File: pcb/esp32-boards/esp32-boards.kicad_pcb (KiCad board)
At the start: 2 copper layers, 55 x 48 mm, 45 parts, among them J1 BOOT_MODE, J2 USB_B_Micro, J3 BATTERY, Q1 Q_Photo_NPN, SW1 RESET, SW2 BAT_EN, U1 ESP32-C3-WROOM-02, U2 MAX40200AUK, U3 MCP73831-2-OT, U4 LD39150DT33

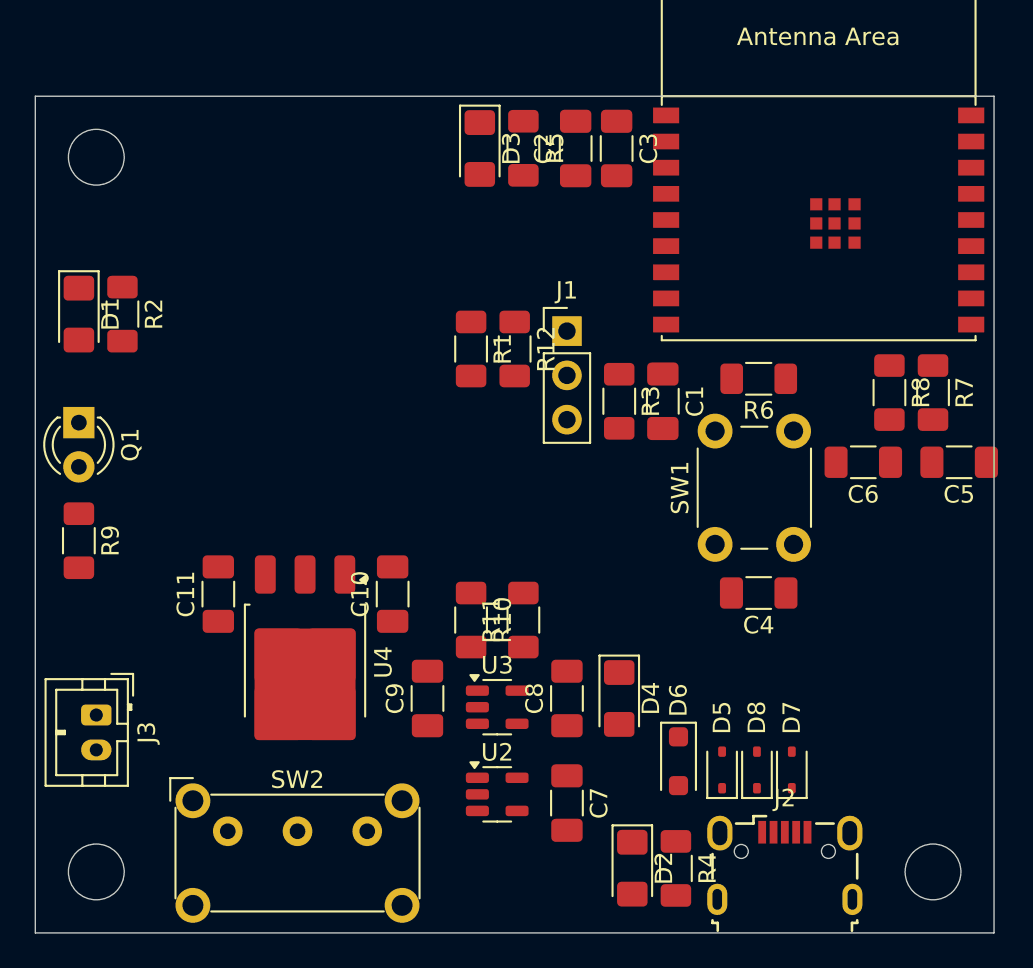
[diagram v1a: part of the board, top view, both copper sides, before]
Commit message: switch to 0805 for most components
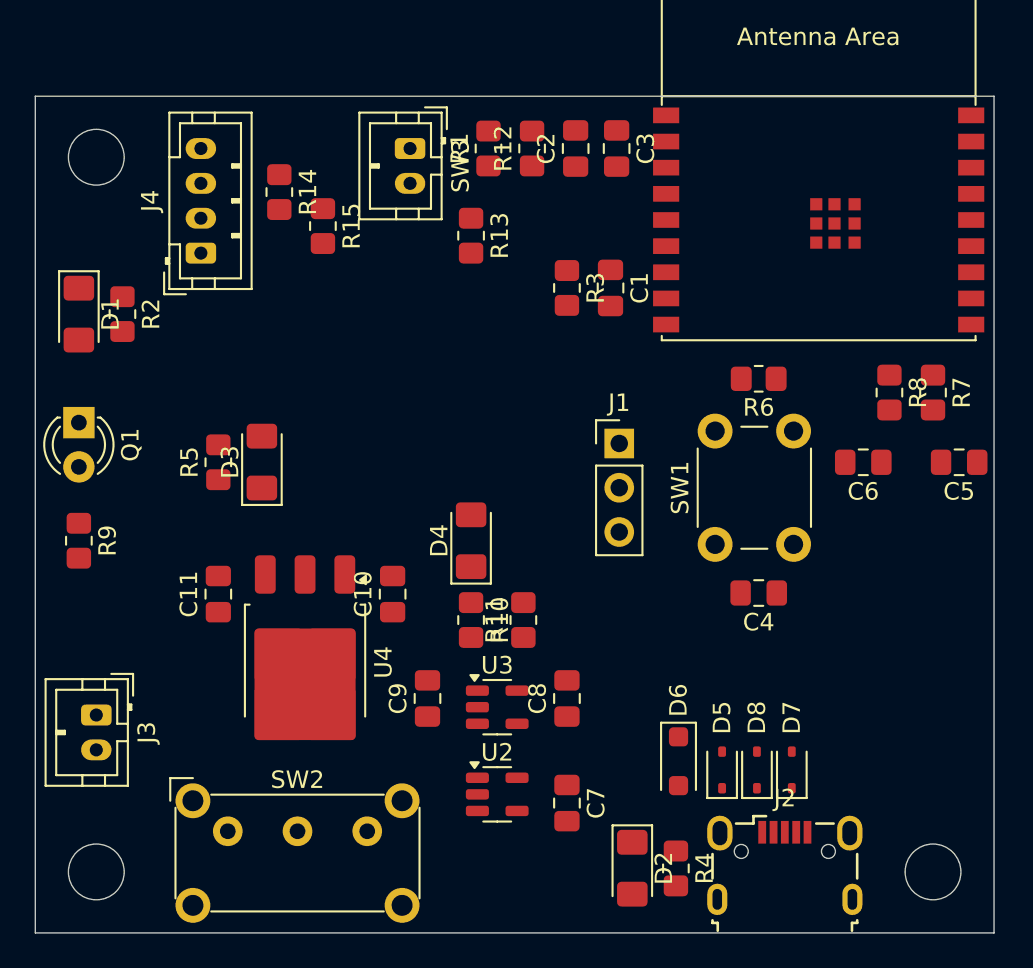
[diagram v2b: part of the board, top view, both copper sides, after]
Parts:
- added J4: LCD, Connector_JST:JST_PH_B4B-PH-K_1x04_P2.00mm_Vertical, F.Cu at (155.0, 61.0)
- added R13: 10k, Resistor_SMD:R_0805_2012Metric_Pad1.20x1.40mm_HandSolder, F.Cu at (170.5, 60.0)
- added R14: 4.7k, Resistor_SMD:R_0805_2012Metric_Pad1.20x1.40mm_HandSolder, F.Cu at (159.5, 57.5)
- added R15: 4.7k, Resistor_SMD:R_0805_2012Metric_Pad1.20x1.40mm_HandSolder, F.Cu at (162.0, 59.5)
- added SW3: READY, Connector_JST:JST_PH_B2B-PH-K_1x02_P2.00mm_Vertical, F.Cu at (167.0, 55.0)
- C1, C10, C11, C2, C3, C4, C5, C6, C7, C8, C9: footprint Capacitor_SMD:C_1206_3216Metric_Pad1.33x1.80mm_HandSolder -> Capacitor_SMD:C_0805_2012Metric_Pad1.18x1.45mm_HandSolder
- R1, R10, R11, R12, R2, R3, R4, R5, R6, R7, R8, R9: footprint Resistor_SMD:R_1206_3216Metric_Pad1.30x1.75mm_HandSolder -> Resistor_SMD:R_0805_2012Metric_Pad1.20x1.40mm_HandSolder
- moved R5 25.1 mm to (156.0, 73.0), turned to 90 degrees
- moved D3 21.9 mm to (158.5, 73.0), turned to 90 degrees
- moved D4 12.4 mm to (170.5, 77.5), turned to 90 degrees
- moved R1 11.5 mm to (171.5, 55.0), turned to 90 degrees
- moved R12 11.5 mm to (174.0, 55.0), turned to 90 degrees
- moved C1 7.16 mm to (178.5, 63.0)
- moved R3 7.16 mm to (176.0, 63.0)
- moved J1 7.11 mm to (179.0, 71.9)
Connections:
- U1 pad 4: unconnected-(U1-GPIO5/ADC2_CH0-Pad4) -> /START
- U1 pad 5: unconnected-(U1-GPIO6-Pad5) -> /SCL
- U1 pad 6: unconnected-(U1-GPIO7-Pad6) -> /SDA

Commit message: finish first draft of layout
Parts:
- removed J1: BOOT_MODE, Connector_PinHeader_2.54mm:PinHeader_1x03_P2.54mm_Vertical
- removed the REF** at (195.0, 36.0)
- added C12: 0.1uF, Capacitor_SMD:C_0805_2012Metric_Pad1.18x1.45mm_HandSolder, F.Cu at (168.5, 96.0)
- added SW4: BOOT_MODE, Button_Switch_THT:SW_PUSH_6mm_H4.3mm, F.Cu at (188.8, 78.8)
- D1: value HEARTBEAT -> STATUS
- D4: value CHARGING -> CHARGE
- SW2: value BAT_EN -> BATTERY_EN
- SW3: value READY -> START
- moved R2 39.9 mm to (185.5, 83.8), turned to 180 degrees
- moved D1 38.2 mm to (181.0, 83.8), turned to 0 degrees
- moved C4 26.7 mm to (162.5, 70.0), turned to -90 degrees
- moved R1 24.6 mm to (159.5, 76.5), turned to 180 degrees
- moved R12 24.3 mm to (159.5, 74.5), turned to 180 degrees
- moved SW1 13.2 mm to (171.8, 74.2), turned to 180 degrees
- moved R6 12.6 mm to (174.5, 70.0), turned to 90 degrees
- moved D3 11.0 mm to (151.0, 81.0), turned to -90 degrees
- moved R5 8.38 mm to (153.5, 81.0), turned to -90 degrees
- moved D8 8.24 mm to (195.1, 91.5), turned to 0 degrees
- moved R7 6.58 mm to (196.0, 75.5)
- moved R8 6.52 mm to (194.0, 75.5)
- moved R14 6.31 mm to (161.8, 63.4)
- moved R15 6.15 mm to (163.8, 65.3)
- moved U1 5.90 mm to (190.4, 64.9)
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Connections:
- net Net-(U1-GPIO18/USB_D-) renamed /D+
- net Net-(U1-GPIO19/USB_D+) renamed /D-
- U1 pad 17: /~{LASER_TRIPPED} -> /HEARTBEAT
- U1 pad 18: /HEARTBEAT -> /~{LASER_TRIPPED}
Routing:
- net /~{LASER_TRIPPED}: track 0.00 -> 62.7 mm, vias 0 -> 2
- net /IO2: track 0.00 -> 55.7 mm
- net /HEARTBEAT: track 0.00 -> 34.8 mm, vias 0 -> 2
- net /SDA: track 0.00 -> 29.7 mm
- net /SCL: track 0.00 -> 29.7 mm
- net /USB_D-: track 0.00 -> 28.8 mm
- net /USB_D+: track 0.00 -> 27.7 mm
- net GND: track 0.00 -> 27.5 mm, vias 0 -> 46
- net /IO8: track 0.00 -> 26.9 mm
- net /EN: track 0.00 -> 22.7 mm, vias 0 -> 2
- net /START: track 0.00 -> 15.0 mm
- net Net-(SW2-B): track 0.00 -> 13.6 mm
- net /D-: track 0.00 -> 13.1 mm
- net /IO9: track 0.00 -> 13.1 mm
- net Net-(C4-Pad1): track 0.00 -> 12.8 mm
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- added copper zone on F.Cu, net +3V3
- added copper zone on B.Cu, net GND
- added copper zone on F.Cu, net GND
- added copper zone on B.Cu, net VBAT
- added copper zone on F.Cu, net VBAT
- added copper zone on B.Cu, net VDD
- added copper zone on F.Cu, net VDD
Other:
- board size 55 x 48 mm -> 55 x 42 mm
- board text added: "3V3"
- board text added: "GND"
- board text added: "SCL"
- board text added: "SDA"
- board text added: "VBAT"

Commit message: add screenshot of differential impedance calculation
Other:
- board text added: "USB differential pair impedance calucation from JLC"

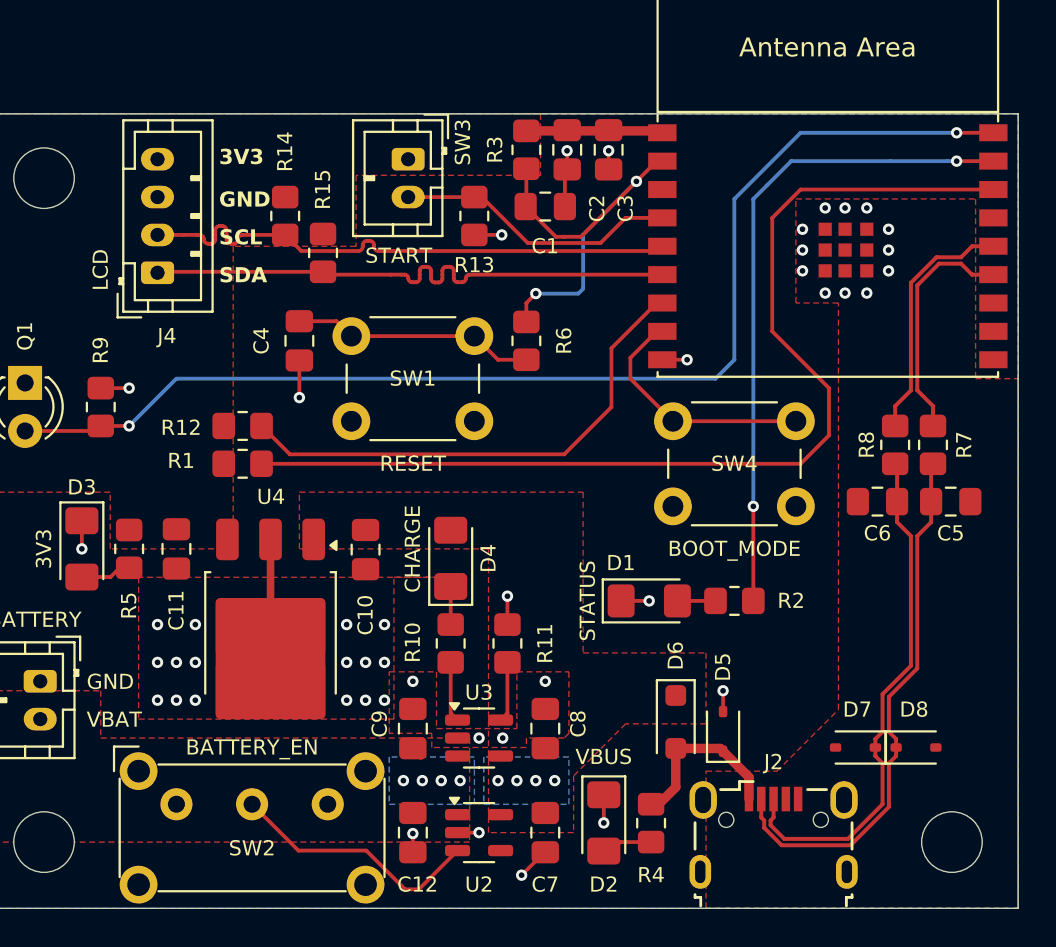
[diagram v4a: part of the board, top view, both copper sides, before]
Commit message: update reference designators
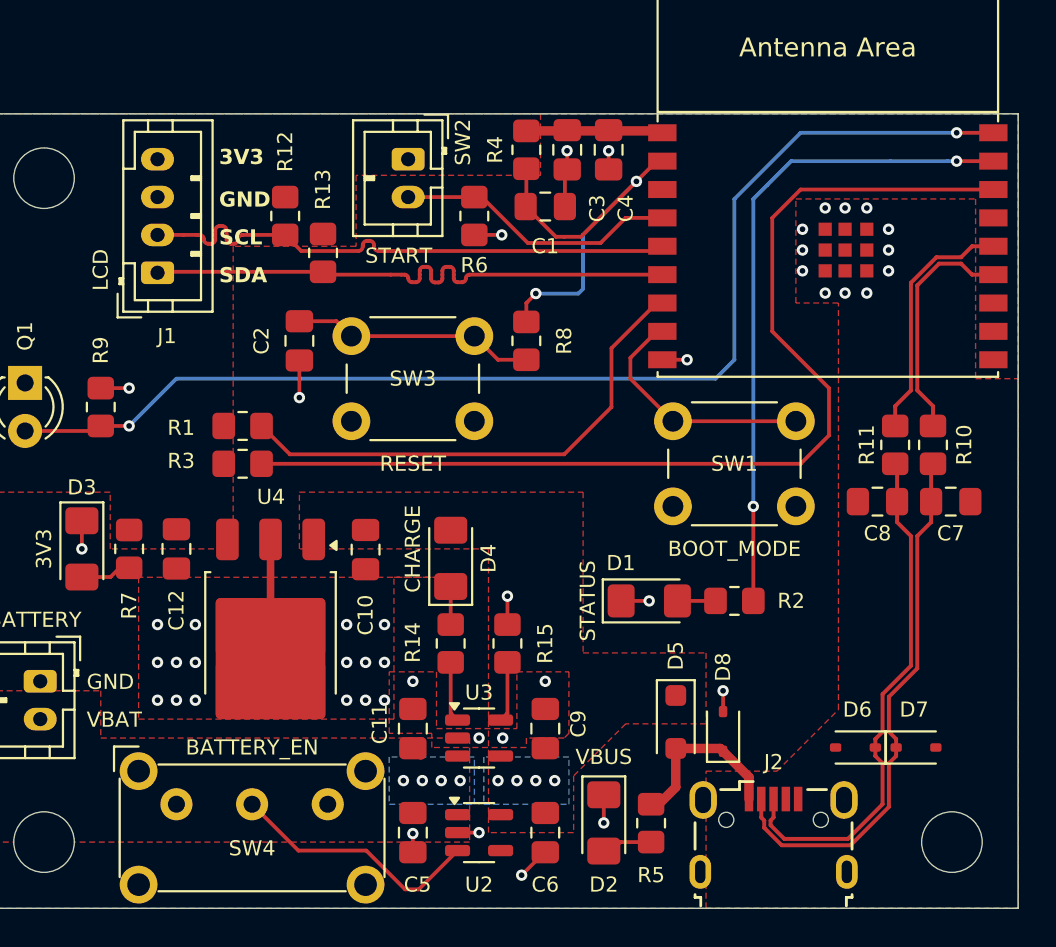
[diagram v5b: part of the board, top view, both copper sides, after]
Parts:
- renumbered C9 to C11, C11 to C12, C4 to C2, C2 to C3, C3 to C4, C12 to C5, C7 to C6, C5 to C7, C6 to C8, C8 to C9, D6 to D5, D7 to D6, D8 to D7, D5 to D8, J4 to J1, R12 to R1, R7 to R10, R8 to R11, R14 to R12, R15 to R13, R10 to R14, R11 to R15, R1 to R3, R3 to R4, R4 to R5, R13 to R6, R5 to R7, R6 to R8, SW4 to SW1, SW3 to SW2, SW1 to SW3, SW2 to SW4

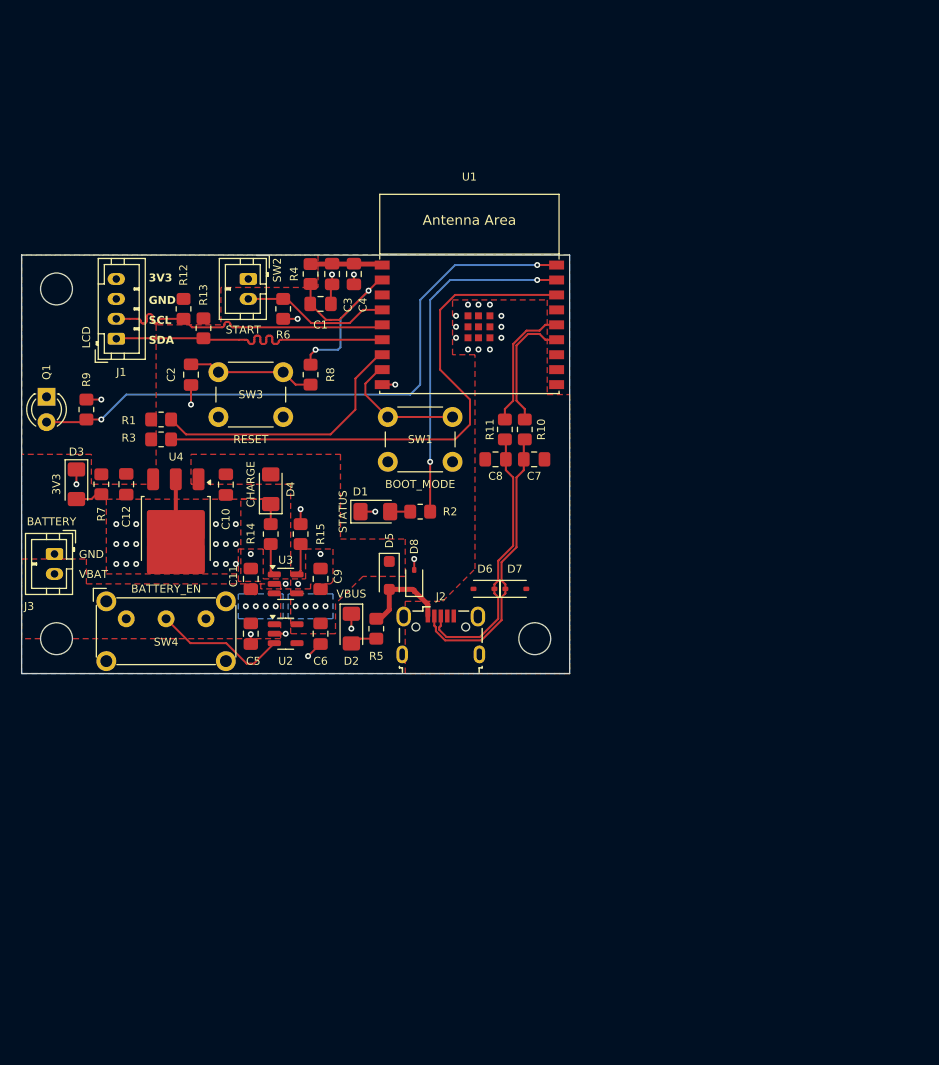
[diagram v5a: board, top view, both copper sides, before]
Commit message: add documentation; move board; resize VBAT pour
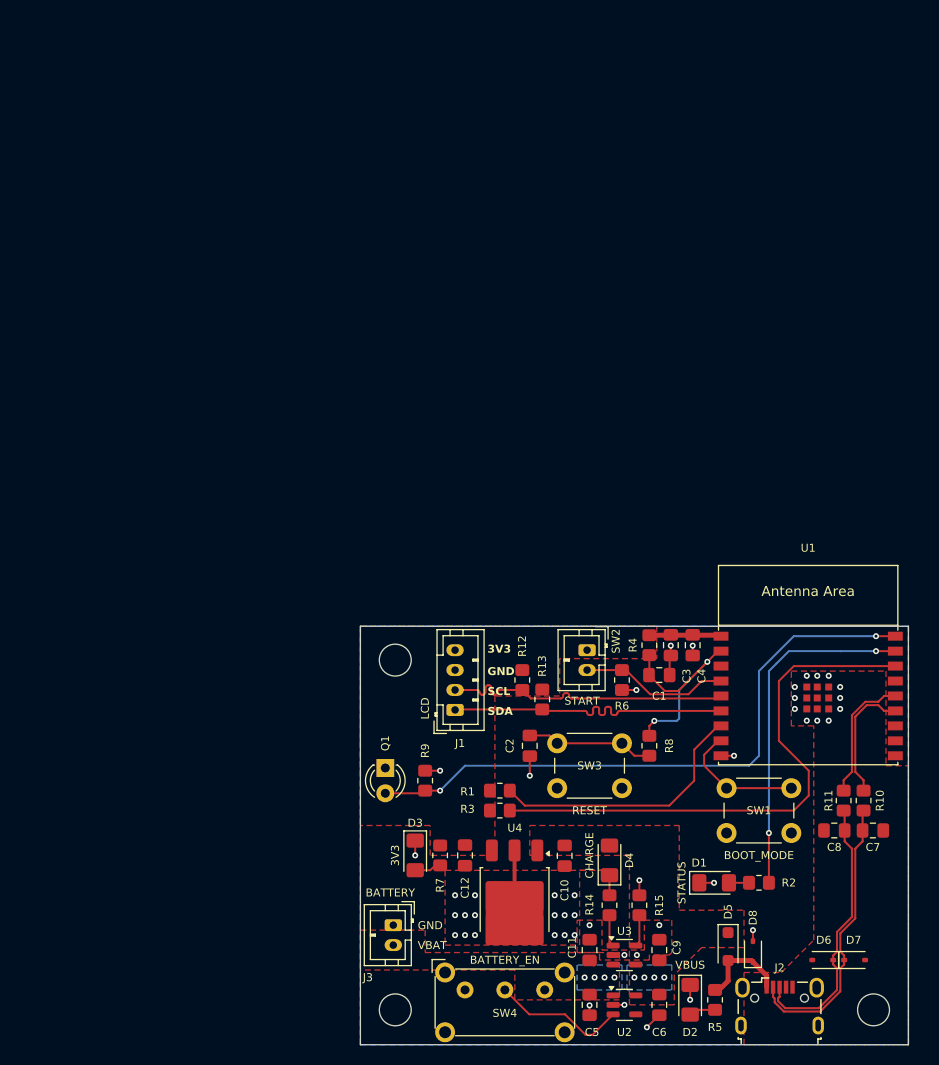
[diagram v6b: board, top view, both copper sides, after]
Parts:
- moved D2 50.4 mm to (212.6, 132.7)
- moved C1 50.4 mm to (209.5, 100.2)
- moved C10 50.4 mm to (200.0, 118.3)
- moved C11 50.4 mm to (202.5, 127.8)
- moved C12 50.4 mm to (190.0, 118.2)
- moved C2 50.4 mm to (196.5, 107.2)
- moved C3 50.4 mm to (210.7, 97.2)
- moved C4 50.4 mm to (212.8, 97.2)
- moved C5 50.4 mm to (202.5, 133.2)
- moved C6 50.4 mm to (209.5, 133.2)
- moved C7 50.4 mm to (230.9, 115.8)
- moved C8 50.4 mm to (227.1, 115.8)
- moved C9 50.4 mm to (209.5, 127.8)
- moved D1 50.4 mm to (215.0, 121.0)
- moved D3 50.4 mm to (185.0, 118.2)
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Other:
- board text added: "I didn't put the battery pack super close to the lipo charger, but that's because I wanted the battery enable switch and the USB connector to be on the same side of the PCB so they can come out of the same side of the enclosure. Not that I couldn't have just made the board a little bit wider :)"
- board text added: "U3 layout based upon recommended layout from datasheet"
